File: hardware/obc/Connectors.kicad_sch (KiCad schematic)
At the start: 16 parts, among them J13 USB_C_Receptacle_USB2.0, J2 Conn_01x05, J3 Conn_01x06, J8 Conn_High-Rel_4S2P, J9 Conn_High-Rel_6P, U7 Mem_MT29F4G01ABAFDWB, U8 Mem_MT29F4G01ABAFDWB

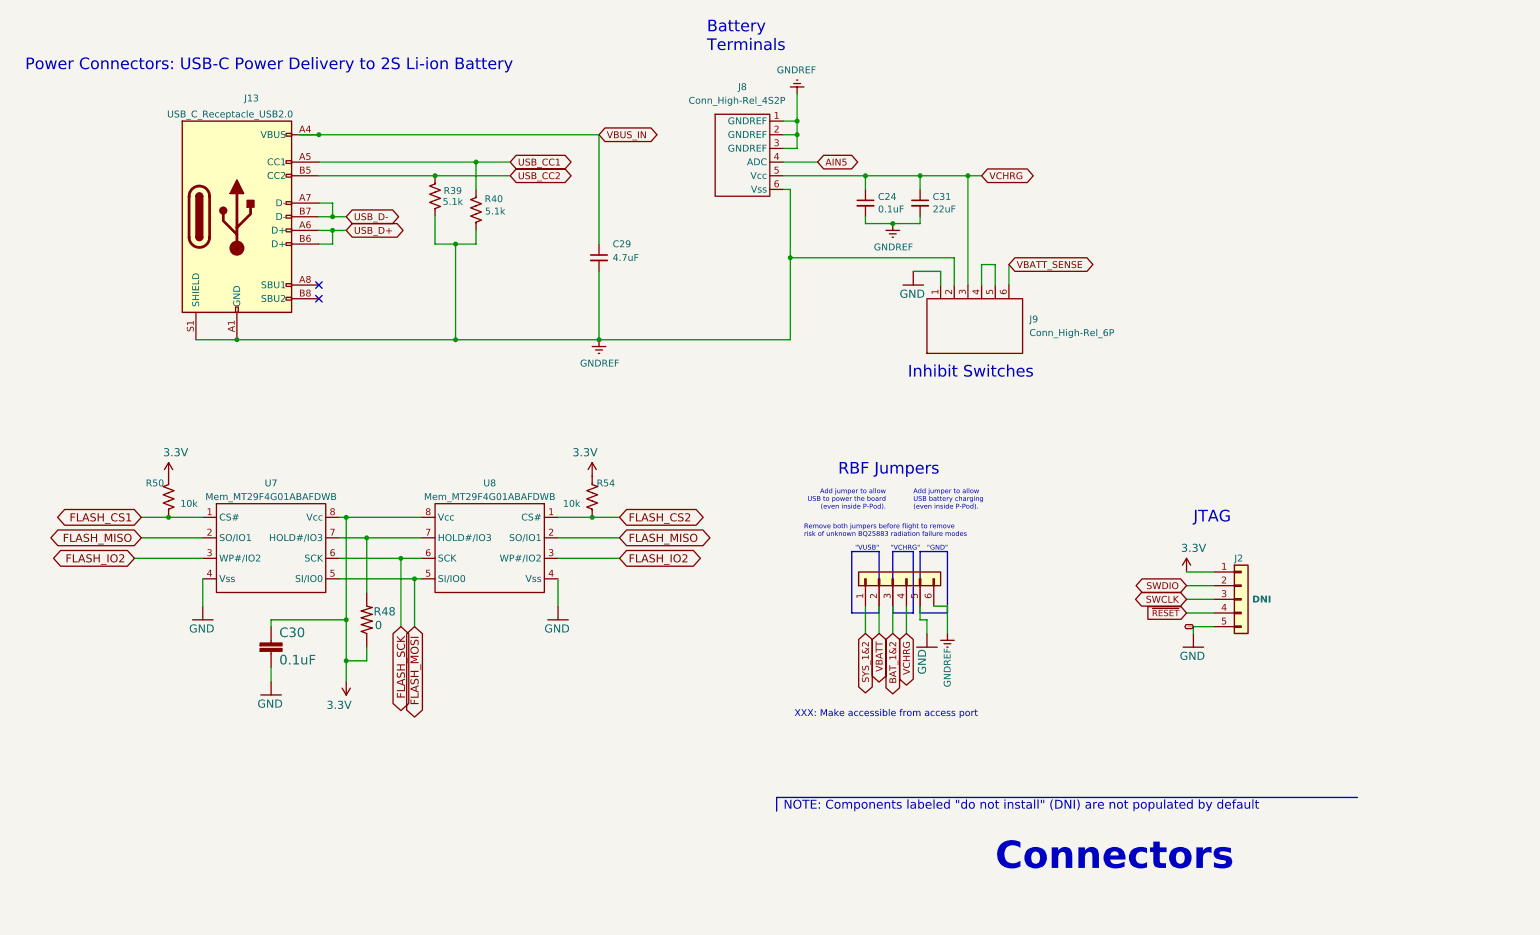
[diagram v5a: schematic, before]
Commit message: obc: footprint editing and schematic revision
Added GPS21+ and edited inductor footprints. Edited schematic circuitry and re-annotated schematic components.
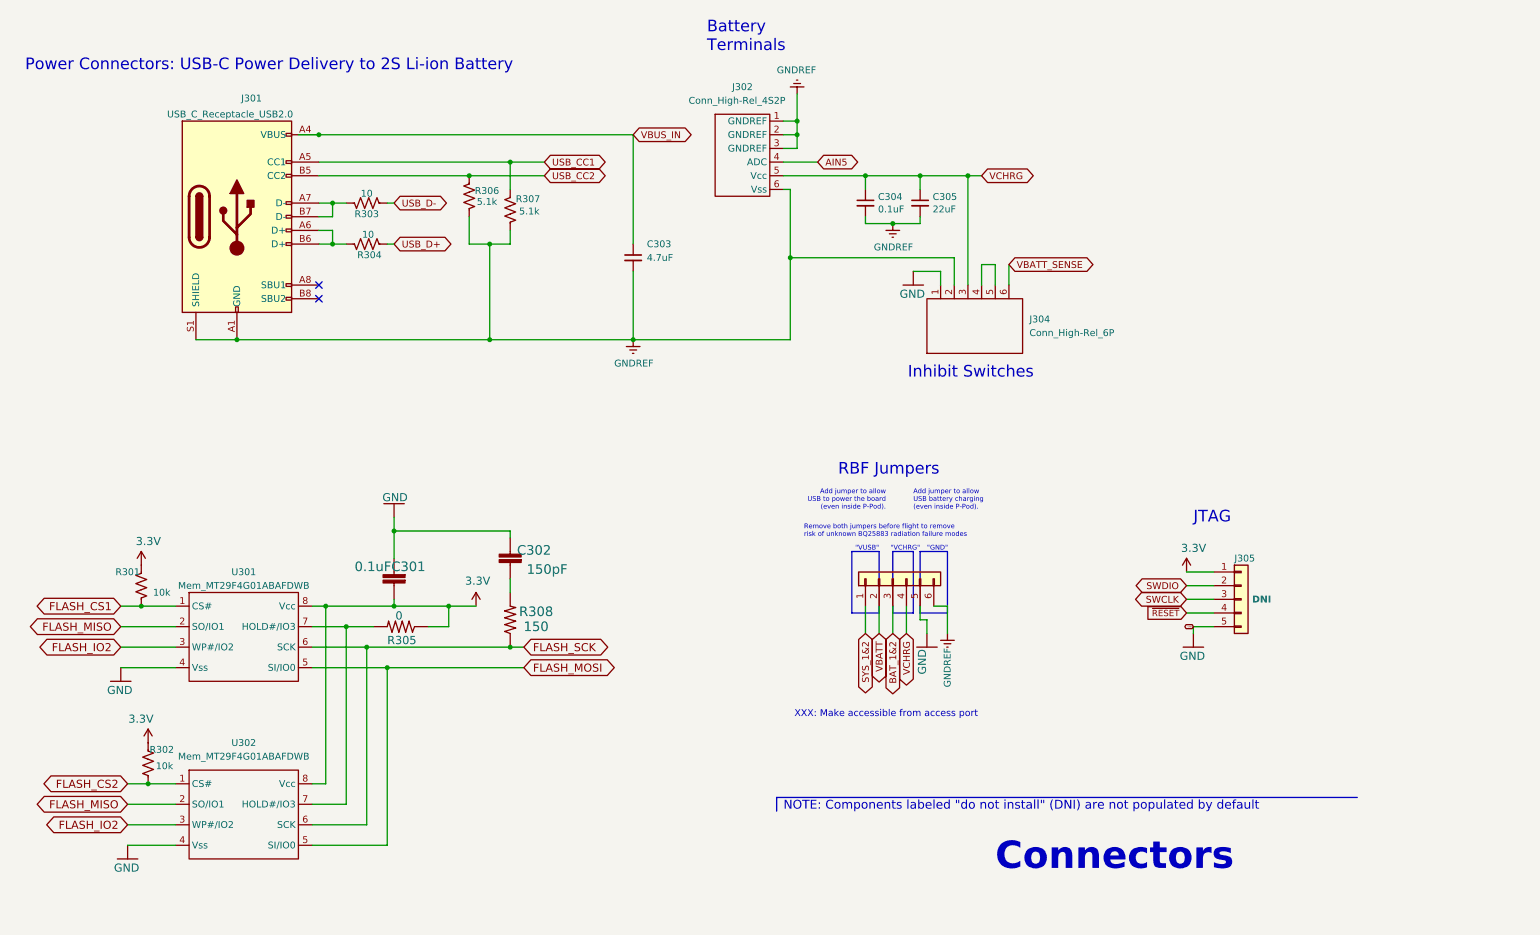
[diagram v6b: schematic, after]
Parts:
- added C302: 150pF, Capacitor_SMD:C_0603_1608Metric, symbol mainboard:2.2UF-0603-10V-20%
- added R303, R304: 10, Resistor_SMD:R_0603_1608Metric, symbol Device:R_US
- added R308: 150, Resistor_SMD:R_0603_1608Metric, symbol mainboard:RESISTOR0603
- renumbered C30 to C301, C29 to C303, C24 to C304, C31 to C305, J13 to J301, J8 to J302, J3 to J303, J9 to J304, J2 to J305, R50 to R301, R54 to R302, R48 to R305, R39 to R306, R40 to R307, U7 to U301, U8 to U302
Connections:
- net FLASH_SCK: now also R308.1
- net GND: now also C302.2
- net USB_D+: now also R304.1; no longer J301.A6 (D+), J301.B6 (D+)
- net USB_D-: now also R303.1; no longer J301.A7 (D-), J301.B7 (D-)
- new net: J301.A6 (D+), J301.B6 (D+), R304.2
- new net: J301.A7 (D-), J301.B7 (D-), R303.2
- new net: C302.1, R308.2
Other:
- moved on the sheet: C301, C303, R301, R302, R305, R306, R307, U301, U302

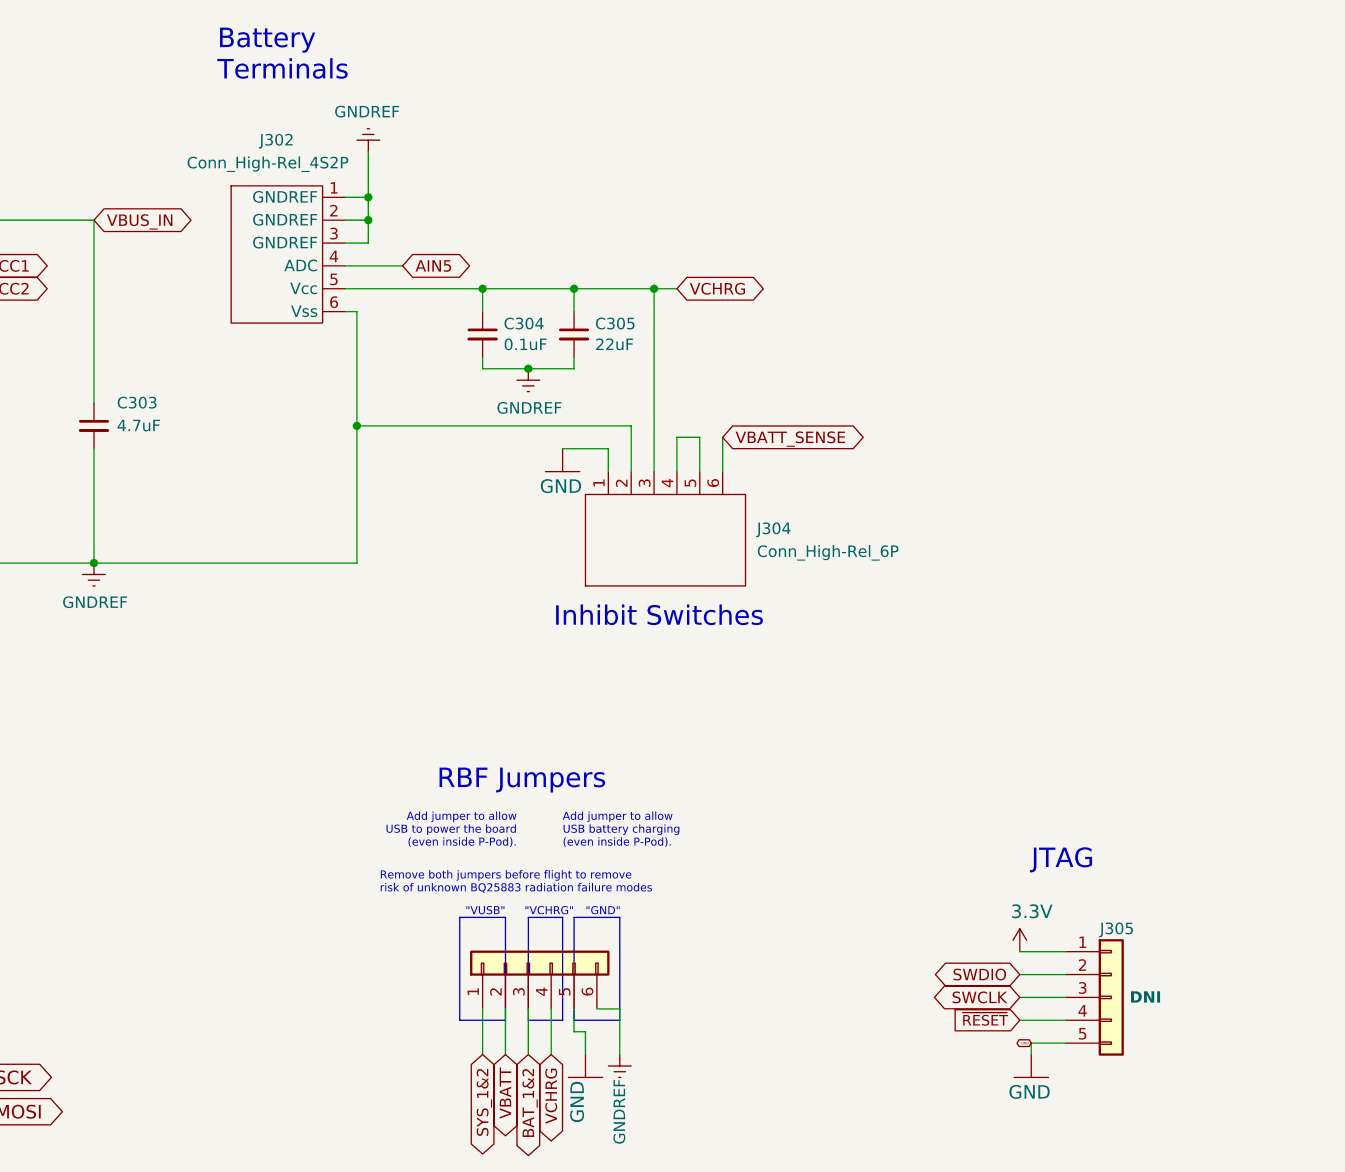
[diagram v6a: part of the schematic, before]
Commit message: obc: BOM editing
Edited the DNI status of several components to be more reflective of our obc setup plans.
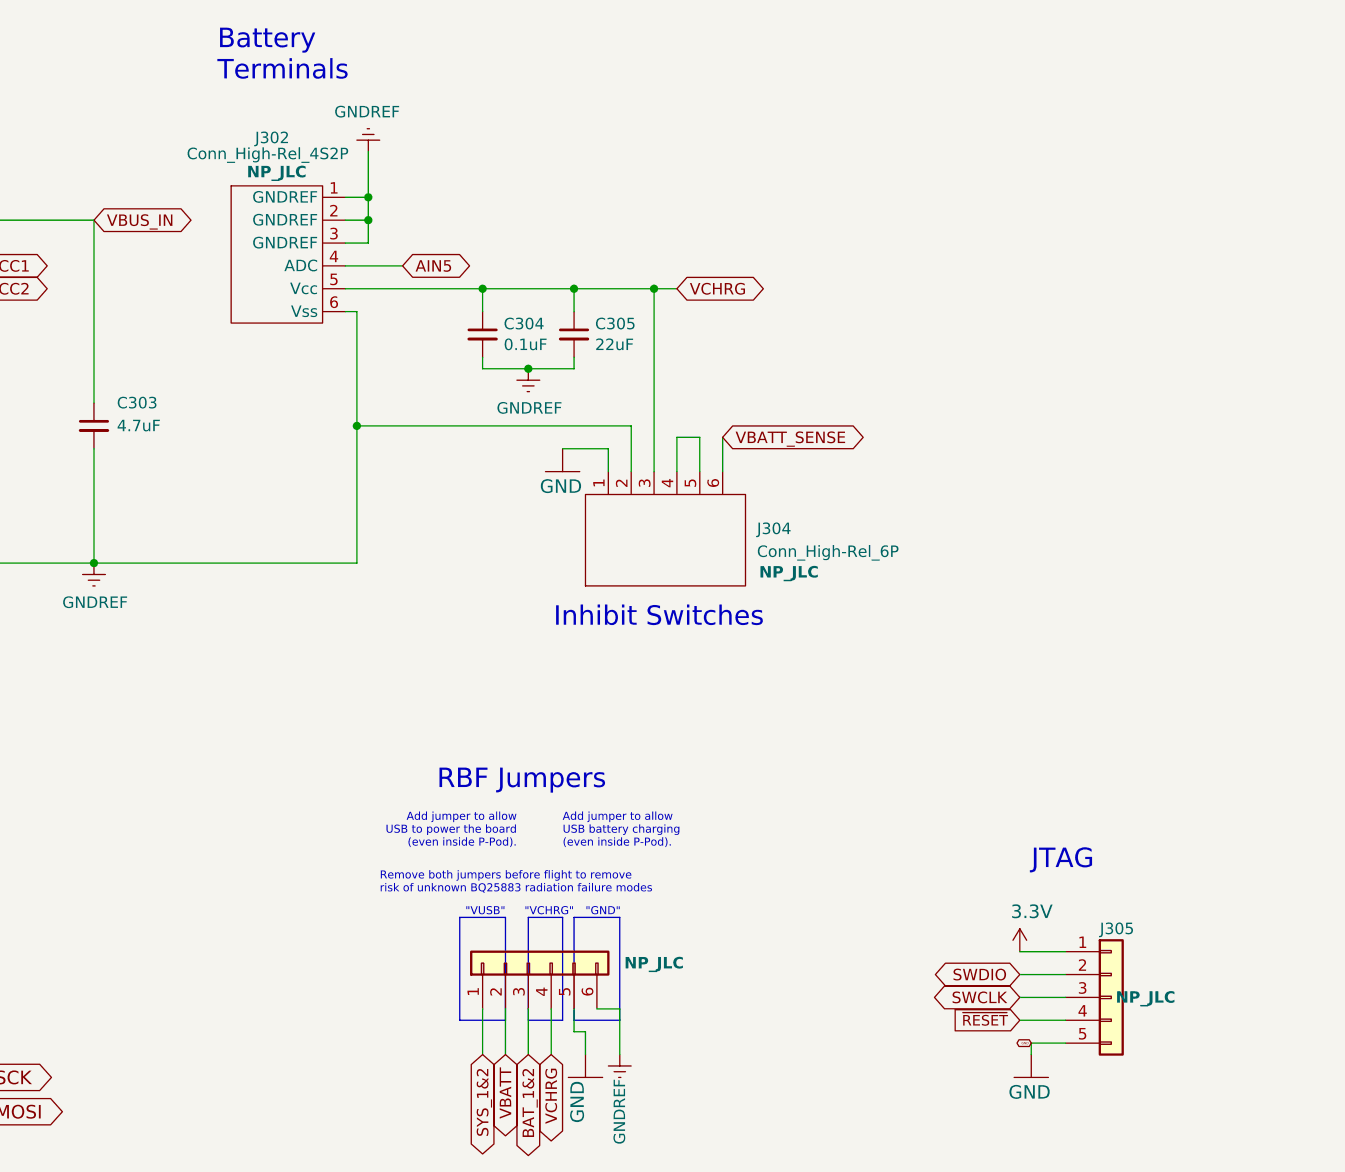
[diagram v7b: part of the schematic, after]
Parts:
- J302, J304: DNI (none) -> NP_JLC
- J303, J305: DNI DNI -> NP_JLC; Notes Not placed by JLCPCB -> (none)
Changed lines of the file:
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@@
 			)
 		)
-		(property "DNI" "DNI"
+		(property "DNI" "NP_JLC"
 			(at 248.92 132.08 0)
 			(effects
@@
 			)
 		)
-		(property "Notes" "Not placed by JLCPCB"
+		(property "Notes" ""
 			(at 245.11 132.08 0)
 			(effects
@@
 		(dnp no)
 		(property "Reference" "J302"
-			(at 152.4 36.83 0)
+			(at 151.892 36.576 0)
 			(effects
 				(font
@@
 		)
 		(property "Value" "Conn_High-Rel_4S2P"
-			(at 151.384 39.37 0)
+			(at 151.384 38.354 0)
 			(effects
 				(font
@@
 			)
 		)
+		(property "DNI" "NP_JLC"
+			(at 155.702 39.624 0)
+			(effects
+				(font
+					(size 1.27 1.27)
+					(bold yes)
+				)
+				(justify right top)
+			)
+		)
 		(pin "3"
 		)
@@
 			)
 		)
-		(property "DNI" "DNI"
+		(property "DNI" "NP_JLC"
 			(at 194.31 128.27 90)
 			(effects
@@
 					(bold yes)
 				)
-				(hide yes)
 			)
 		)
@@
 			)
 		)
-		(property "Notes" "Not placed by JLCPCB"
+		(property "Notes" ""
 			(at 180.34 128.27 0)
 			(effects
@@
 		(on_board yes)
 		(dnp no)
-		(fields_autoplaced yes)
 		(property "Reference" "J304"
 			(at 205.74 80.0099 90)
@@
 			)
 		)
+		(property "DNI" "NP_JLC"
+			(at 209.296 84.836 90)
+			(effects
+				(font
+					(size 1.27 1.27)
+					(bold yes)
+				)
+			)
+		)

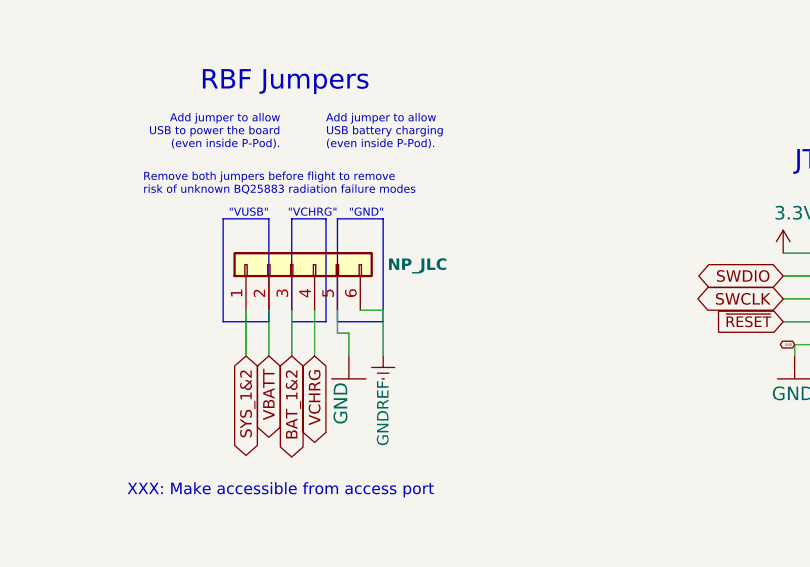
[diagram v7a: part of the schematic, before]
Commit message: obc: preliminary board layout
Entered design rules and grouped components according to schematic. Slightly edited BOM.
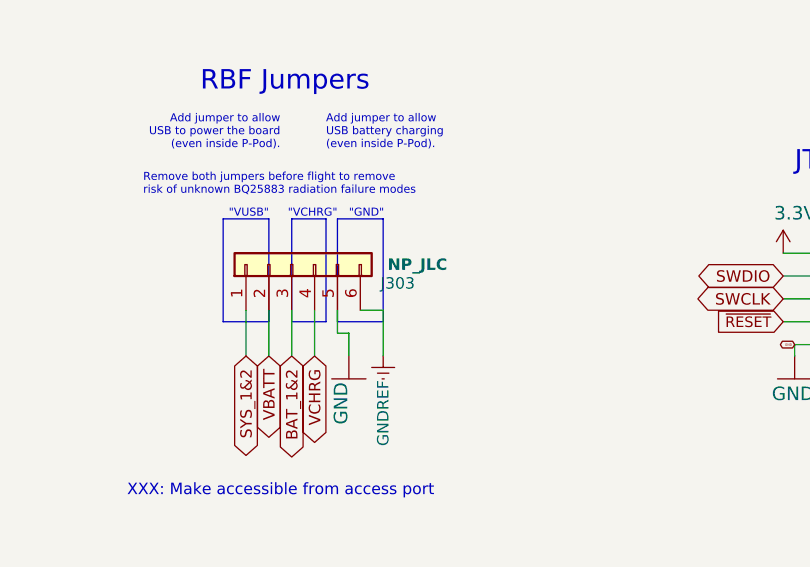
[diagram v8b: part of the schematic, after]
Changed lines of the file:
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@@
 				)
 				(justify right)
-				(hide yes)
 			)
 		)
